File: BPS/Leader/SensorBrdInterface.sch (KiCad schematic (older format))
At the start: 15 parts, among them J7 MinionConn, J8 CurrentConn, U5 LTC6820, U6 LTC6820, U7 HX1188FNL

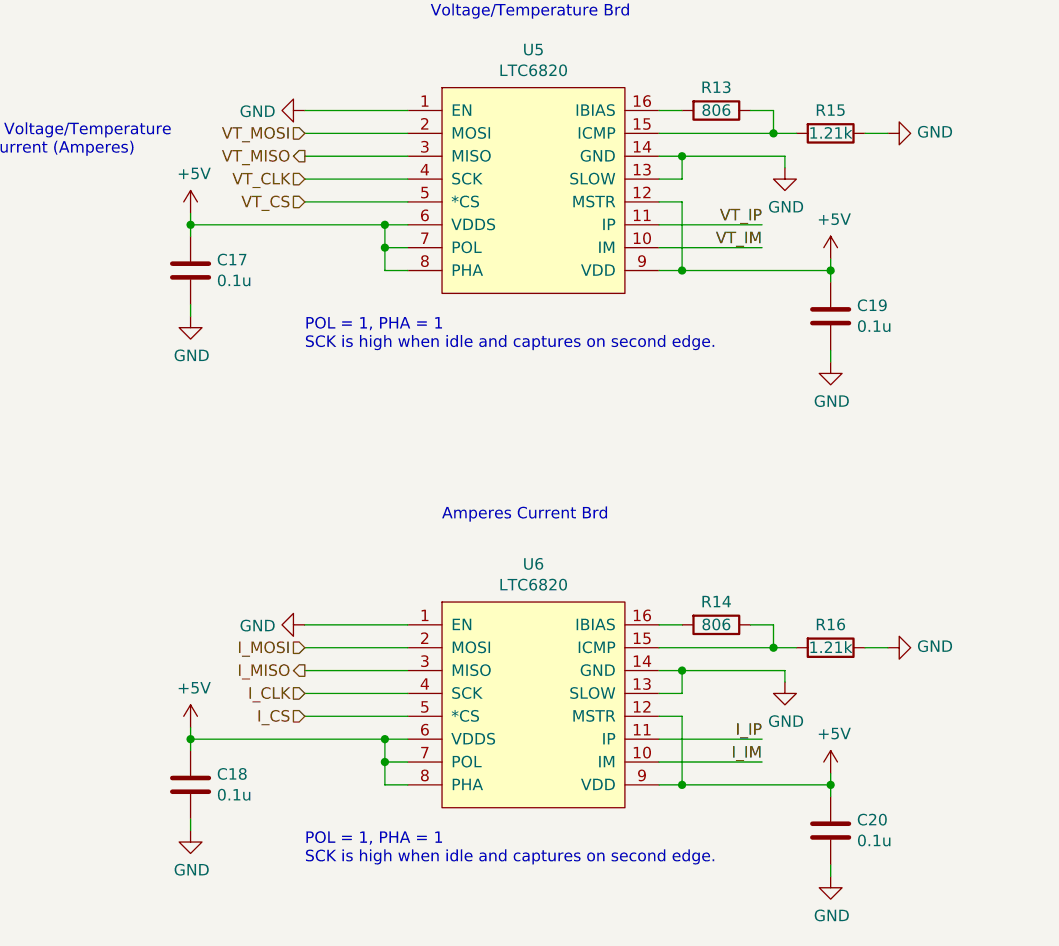
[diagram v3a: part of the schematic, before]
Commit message: Simplifies dc-dc converter schematics
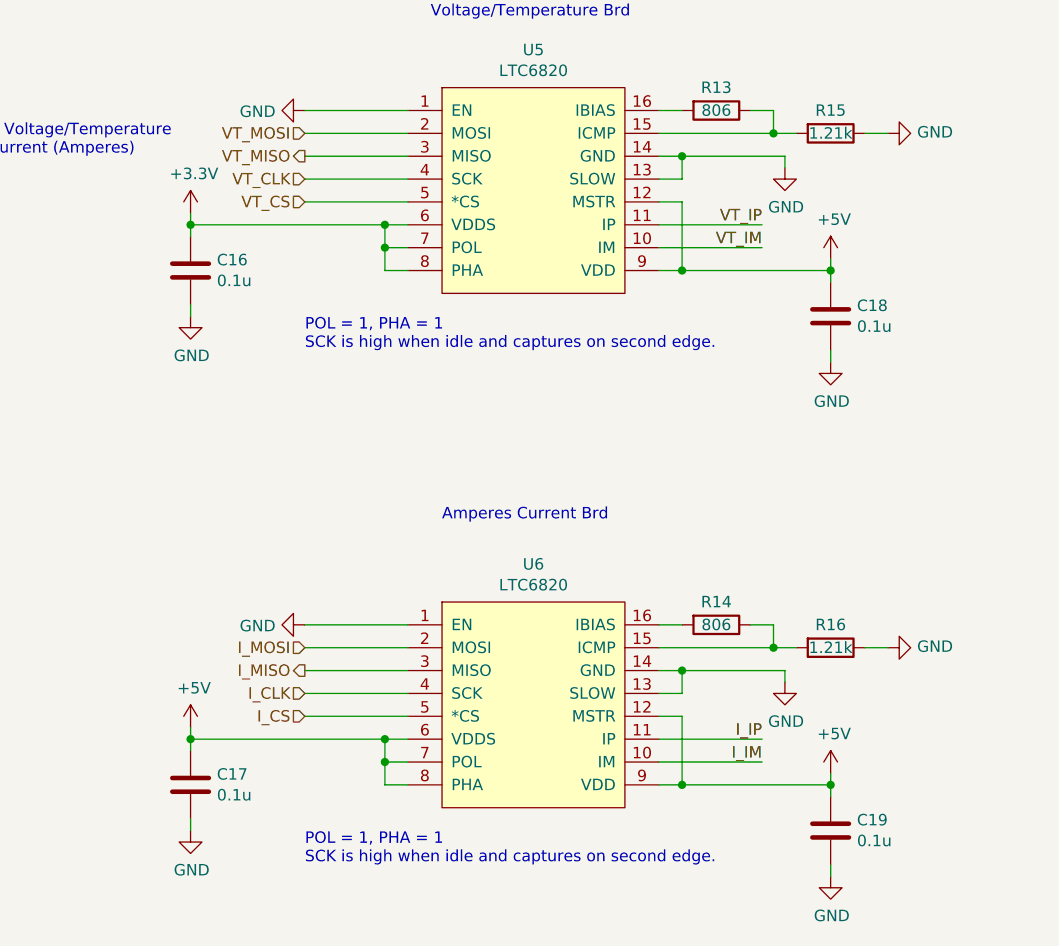
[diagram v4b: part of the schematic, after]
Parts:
- renumbered C17 to C16, C18 to C17, C19 to C18, C20 to C19
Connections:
- net +5V: no longer C16.1, U5.6 (VDDS), U5.7 (POL), U5.8 (PHA)
- new net +3V3: C16.1, U5.6 (VDDS), U5.7 (POL), U5.8 (PHA)
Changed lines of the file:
@@
 P 4650 2800
 AR Path="/5C4C7509/5D76E53B" Ref="#PWR?"  Part="1"
-AR Path="/5D766247/5D76E53B" Ref="#PWR041"  Part="1"
-F 0 "#PWR041" H 4650 2550 50  0001 C CNN
+AR Path="/5D766247/5D76E53B" Ref="#PWR040"  Part="1"
+F 0 "#PWR040" H 4650 2550 50  0001 C CNN
 F 1 "GND" H 4655 2627 50  0000 C CNN
 F 2 "" H 4650 2800 50  0001 C CNN
@@
 P 2550 2550
 AR Path="/5C4C7509/5D76E546" Ref="#PWR?"  Part="1"
-AR Path="/5D766247/5D76E546" Ref="#PWR039"  Part="1"
-F 0 "#PWR039" H 2550 2300 50  0001 C CNN
+AR Path="/5D766247/5D76E546" Ref="#PWR038"  Part="1"
+F 0 "#PWR038" H 2550 2300 50  0001 C CNN
 F 1 "GND" V 2555 2422 50  0000 R CNN
 F 2 "" H 2550 2550 50  0001 C CNN
@@
 P 2050 3250
 AR Path="/5C4C7509/5D76E54F" Ref="C?"  Part="1"
-AR Path="/5D766247/5D76E54F" Ref="C17"  Part="1"
-F 0 "C17" H 2165 3296 50  0000 L CNN
+AR Path="/5D766247/5D76E54F" Ref="C16"  Part="1"
+F 0 "C16" H 2165 3296 50  0000 L CNN
 F 1 "0.1u" H 2165 3205 50  0000 L CNN
 F 2 "Capacitor_SMD:C_0805_2012Metric" H 2088 3100 50  0001 C CNN
@@
 P 2050 3450
 AR Path="/5C4C7509/5D76E556" Ref="#PWR?"  Part="1"
-AR Path="/5D766247/5D76E556" Ref="#PWR036"  Part="1"
-F 0 "#PWR036" H 2050 3200 50  0001 C CNN
+AR Path="/5D766247/5D76E556" Ref="#PWR035"  Part="1"
+F 0 "#PWR035" H 2050 3200 50  0001 C CNN
 F 1 "GND" H 2055 3277 50  0000 C CNN
 F 2 "" H 2050 3450 50  0001 C CNN
@@
 P 4850 3450
 AR Path="/5C4C7509/5D76E56F" Ref="C?"  Part="1"
-AR Path="/5D766247/5D76E56F" Ref="C19"  Part="1"
-F 0 "C19" H 4965 3496 50  0000 L CNN
+AR Path="/5D766247/5D76E56F" Ref="C18"  Part="1"
+F 0 "C18" H 4965 3496 50  0000 L CNN
 F 1 "0.1u" H 4965 3405 50  0000 L CNN
 F 2 "Capacitor_SMD:C_0805_2012Metric" H 4888 3300 50  0001 C CNN
@@
 P 4850 3650
 AR Path="/5C4C7509/5D76E575" Ref="#PWR?"  Part="1"
-AR Path="/5D766247/5D76E575" Ref="#PWR044"  Part="1"
-F 0 "#PWR044" H 4850 3400 50  0001 C CNN
+AR Path="/5D766247/5D76E575" Ref="#PWR043"  Part="1"
+F 0 "#PWR043" H 4850 3400 50  0001 C CNN
 F 1 "GND" H 4855 3477 50  0000 C CNN
 F 2 "" H 4850 3650 50  0001 C CNN
@@
 P 5100 2650
 AR Path="/5C4C7509/5D76E58F" Ref="#PWR?"  Part="1"
-AR Path="/5D766247/5D76E58F" Ref="#PWR047"  Part="1"
-F 0 "#PWR047" H 5100 2400 50  0001 C CNN
+AR Path="/5D766247/5D76E58F" Ref="#PWR046"  Part="1"
+F 0 "#PWR046" H 5100 2400 50  0001 C CNN
 F 1 "GND" V 5105 2522 50  0000 R CNN
 F 2 "" H 5100 2650 50  0001 C CNN
@@
 P 4850 3200
 AR Path="/5C4C7509/5D76E5AC" Ref="#PWR?"  Part="1"
-AR Path="/5D766247/5D76E5AC" Ref="#PWR043"  Part="1"
-F 0 "#PWR043" H 4850 3050 50  0001 C CNN
+AR Path="/5D766247/5D76E5AC" Ref="#PWR042"  Part="1"
+F 0 "#PWR042" H 4850 3050 50  0001 C CNN
 F 1 "+5V" H 4865 3373 50  0000 C CNN
 F 2 "" H 4850 3200 50  0001 C CNN
@@
 Wire Wire Line
 	7100 3500 7500 3500
-$Comp
-L power:+5V #PWR?
-U 1 1 5D76E5D1
-P 2050 3000
-AR Path="/5C4C7509/5D76E5D1" Ref="#PWR?"  Part="1"
-AR Path="/5D766247/5D76E5D1" Ref="#PWR035"  Part="1"
-F 0 "#PWR035" H 2050 2850 50  0001 C CNN
-F 1 "+5V" H 2065 3173 50  0000 C CNN
-F 2 "" H 2050 3000 50  0001 C CNN
-F 3 "" H 2050 3000 50  0001 C CNN
-	1    2050 3000
-	1    0    0    -1
-$EndComp
 Wire Wire Line
 	2050 3000 2050 3050
@@
 P 4650 5050
 AR Path="/5C4C7509/5F151E6E" Ref="#PWR?"  Part="1"
-AR Path="/5D766247/5F151E6E" Ref="#PWR042"  Part="1"
-F 0 "#PWR042" H 4650 4800 50  0001 C CNN
+AR Path="/5D766247/5F151E6E" Ref="#PWR041"  Part="1"
+F 0 "#PWR041" H 4650 4800 50  0001 C CNN
 F 1 "GND" H 4655 4877 50  0000 C CNN
 F 2 "" H 4650 5050 50  0001 C CNN
@@
 P 2550 4800
 AR Path="/5C4C7509/5F151E76" Ref="#PWR?"  Part="1"
-AR Path="/5D766247/5F151E76" Ref="#PWR040"  Part="1"
-F 0 "#PWR040" H 2550 4550 50  0001 C CNN
+AR Path="/5D766247/5F151E76" Ref="#PWR039"  Part="1"
+F 0 "#PWR039" H 2550 4550 50  0001 C CNN
 F 1 "GND" V 2555 4672 50  0000 R CNN
 F 2 "" H 2550 4800 50  0001 C CNN
@@
 P 2050 5500
 AR Path="/5C4C7509/5F151E7F" Ref="C?"  Part="1"
-AR Path="/5D766247/5F151E7F" Ref="C18"  Part="1"
-F 0 "C18" H 2165 5546 50  0000 L CNN
+AR Path="/5D766247/5F151E7F" Ref="C17"  Part="1"
+F 0 "C17" H 2165 5546 50  0000 L CNN
 F 1 "0.1u" H 2165 5455 50  0000 L CNN
 F 2 "Capacitor_SMD:C_0805_2012Metric" H 2088 5350 50  0001 C CNN
@@
 P 2050 5700
 AR Path="/5C4C7509/5F151E86" Ref="#PWR?"  Part="1"
-AR Path="/5D766247/5F151E86" Ref="#PWR038"  Part="1"
-F 0 "#PWR038" H 2050 5450 50  0001 C CNN
+AR Path="/5D766247/5F151E86" Ref="#PWR037"  Part="1"
+F 0 "#PWR037" H 2050 5450 50  0001 C CNN
 F 1 "GND" H 2055 5527 50  0000 C CNN
 F 2 "" H 2050 5700 50  0001 C CNN
@@
 P 4850 5700
 AR Path="/5C4C7509/5F151E9F" Ref="C?"  Part="1"
-AR Path="/5D766247/5F151E9F" Ref="C20"  Part="1"
-F 0 "C20" H 4965 5746 50  0000 L CNN
+AR Path="/5D766247/5F151E9F" Ref="C19"  Part="1"
+F 0 "C19" H 4965 5746 50  0000 L CNN
 F 1 "0.1u" H 4965 5655 50  0000 L CNN
 F 2 "Capacitor_SMD:C_0805_2012Metric" H 4888 5550 50  0001 C CNN
@@
 P 4850 5900
 AR Path="/5C4C7509/5F151EA5" Ref="#PWR?"  Part="1"
-AR Path="/5D766247/5F151EA5" Ref="#PWR046"  Part="1"
-F 0 "#PWR046" H 4850 5650 50  0001 C CNN
+AR Path="/5D766247/5F151EA5" Ref="#PWR045"  Part="1"
+F 0 "#PWR045" H 4850 5650 50  0001 C CNN
 F 1 "GND" H 4855 5727 50  0000 C CNN
 F 2 "" H 4850 5900 50  0001 C CNN
@@
 P 5100 4900
 AR Path="/5C4C7509/5F151EBF" Ref="#PWR?"  Part="1"
-AR Path="/5D766247/5F151EBF" Ref="#PWR048"  Part="1"
-F 0 "#PWR048" H 5100 4650 50  0001 C CNN
+AR Path="/5D766247/5F151EBF" Ref="#PWR047"  Part="1"
+F 0 "#PWR047" H 5100 4650 50  0001 C CNN
 F 1 "GND" V 5105 4772 50  0000 R CNN
 F 2 "" H 5100 4900 50  0001 C CNN
@@
 P 4850 5450
 AR Path="/5C4C7509/5F151EC9" Ref="#PWR?"  Part="1"
-AR Path="/5D766247/5F151EC9" Ref="#PWR045"  Part="1"
-F 0 "#PWR045" H 4850 5300 50  0001 C CNN
+AR Path="/5D766247/5F151EC9" Ref="#PWR044"  Part="1"
+F 0 "#PWR044" H 4850 5300 50  0001 C CNN
 F 1 "+5V" H 4865 5623 50  0000 C CNN
 F 2 "" H 4850 5450 50  0001 C CNN
@@
 P 2050 5250
 AR Path="/5C4C7509/5F151ED3" Ref="#PWR?"  Part="1"
-AR Path="/5D766247/5F151ED3" Ref="#PWR037"  Part="1"
-F 0 "#PWR037" H 2050 5100 50  0001 C CNN
+AR Path="/5D766247/5F151ED3" Ref="#PWR036"  Part="1"
+F 0 "#PWR036" H 2050 5100 50  0001 C CNN
 F 1 "+5V" H 2065 5423 50  0000 C CNN
 F 2 "" H 2050 5250 50  0001 C CNN
@@
 $EndComp
 $Comp
-L power:+12V #PWR049
+L power:+12V #PWR048
 U 1 1 5F1F84DF
 P 9100 4000
-F 0 "#PWR049" H 9100 3850 50  0001 C CNN
+F 0 "#PWR048" H 9100 3850 50  0001 C CNN
 F 1 "+12V" H 9115 4173 50  0000 C CNN
 F 2 "" H 9100 4000 50  0001 C CNN
@@
 $EndComp
 $Comp
-L power:GNDPWR #PWR050
+L power:GNDPWR #PWR049
 U 1 1 5F1F8DBA
 P 9100 4500
-F 0 "#PWR050" H 9100 4300 50  0001 C CNN
+F 0 "#PWR049" H 9100 4300 50  0001 C CNN
 F 1 "GNDPWR" H 9104 4346 50  0000 C CNN
 F 2 "" H 9100 4450 50  0001 C CNN
@@
 Text Notes 2650 1900 0    50   ~ 10
 4-wire SPI to 2-wire Isolated SPI Converter ICs
+$Comp
+L power:+3.3V #PWR034
+U 1 1 5F1D7210
+P 2050 3000
+F 0 "#PWR034" H 2050 2850 50  0001 C CNN
+F 1 "+3.3V" H 2065 3173 50  0000 C CNN
+F 2 "" H 2050 3000 50  0001 C CNN
+F 3 "" H 2050 3000 50  0001 C CNN
+	1    2050 3000
+	1    0    0    -1
+$EndComp
 $EndSCHEMATC

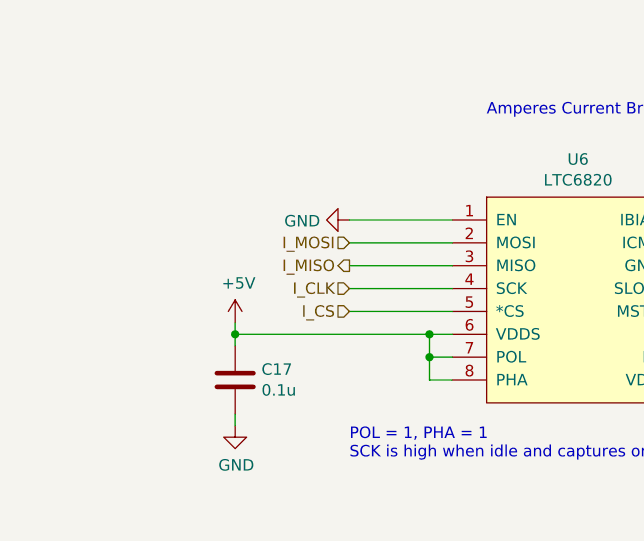
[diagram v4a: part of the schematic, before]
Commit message: Finishes new power circuitry tracing
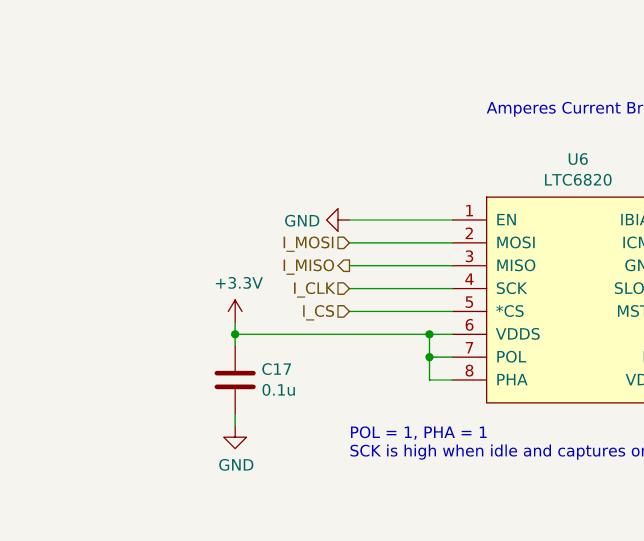
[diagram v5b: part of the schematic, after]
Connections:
- net +3V3: now also C17.1, U6.6 (VDDS), U6.7 (POL), U6.8 (PHA)
- net +5V: no longer C17.1, U6.6 (VDDS), U6.7 (POL), U6.8 (PHA)
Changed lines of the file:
@@
 Wire Wire Line
 	2900 5500 3000 5500
-$Comp
-L power:+5V #PWR?
-U 1 1 5F151ED3
-P 2050 5250
-AR Path="/5C4C7509/5F151ED3" Ref="#PWR?"  Part="1"
-AR Path="/5D766247/5F151ED3" Ref="#PWR036"  Part="1"
-F 0 "#PWR036" H 2050 5100 50  0001 C CNN
-F 1 "+5V" H 2065 5423 50  0000 C CNN
-F 2 "" H 2050 5250 50  0001 C CNN
-F 3 "" H 2050 5250 50  0001 C CNN
-	1    2050 5250
-	1    0    0    -1
-$EndComp
 Wire Wire Line
 	2050 5250 2050 5300
@@
 	1    0    0    -1
 $EndComp
+$Comp
+L power:+3.3V #PWR0104
+U 1 1 5F1DCEE5
+P 2050 5250
+F 0 "#PWR0104" H 2050 5100 50  0001 C CNN
+F 1 "+3.3V" H 2065 5423 50  0000 C CNN
+F 2 "" H 2050 5250 50  0001 C CNN
+F 3 "" H 2050 5250 50  0001 C CNN
+	1    2050 5250
+	1    0    0    -1
+$EndComp

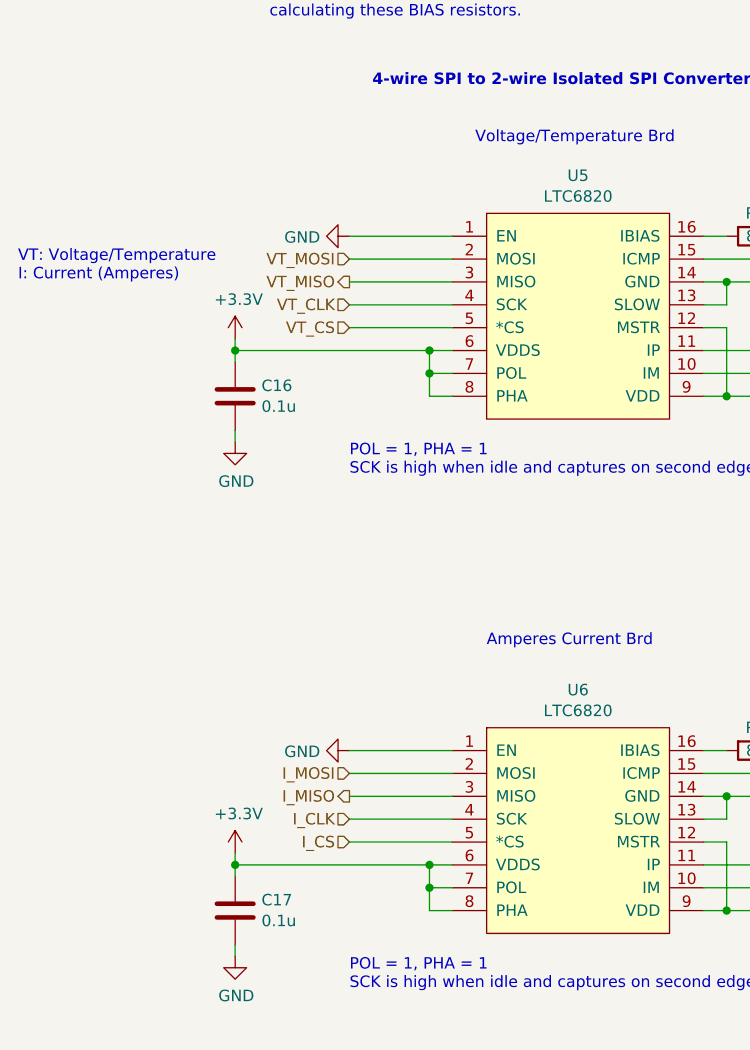
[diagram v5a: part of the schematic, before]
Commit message: Changes LTC6820 POL and PHA pins to +5V due to VIH and VIL parameters in datasheet
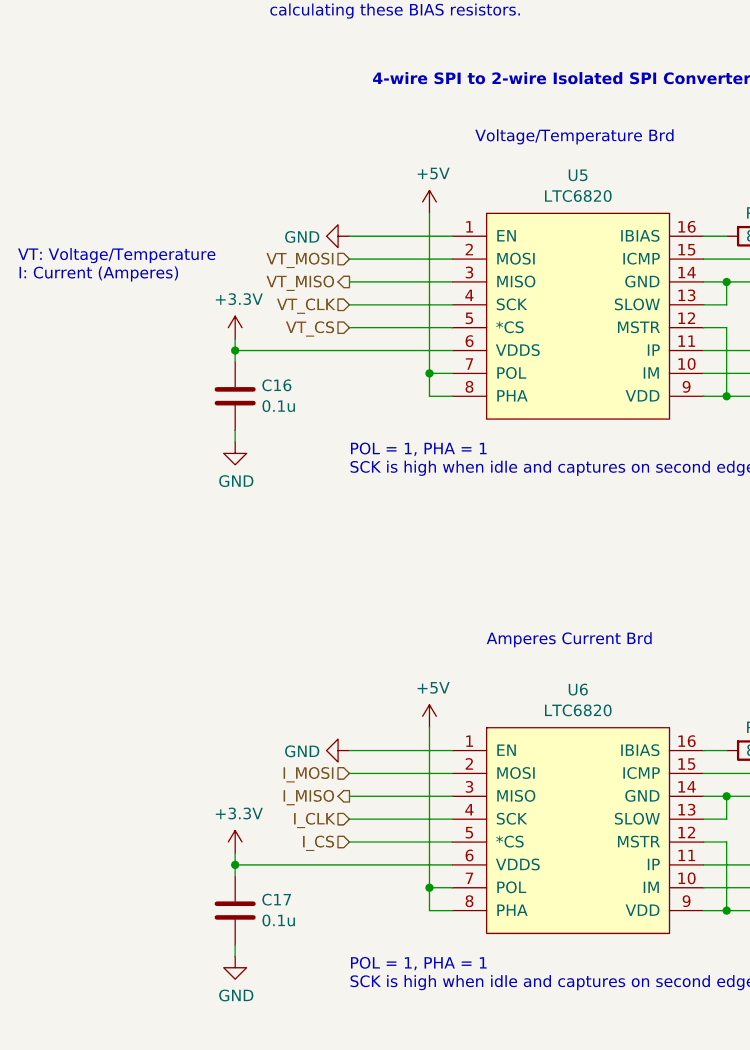
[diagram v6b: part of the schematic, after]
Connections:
- net +3V3: no longer U5.7 (POL), U5.8 (PHA), U6.7 (POL), U6.8 (PHA)
- net +5V: now also U5.7 (POL), U5.8 (PHA), U6.7 (POL), U6.8 (PHA)
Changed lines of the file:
@@
 NoConn ~ 7500 3600
-Wire Wire Line
-	2050 3050 2900 3050
 Wire Wire Line
 	3000 3150 2900 3150
@@
 	2050 3000 2050 3050
 Connection ~ 2050 3050
-Wire Wire Line
-	2900 3150 2900 3050
-Connection ~ 2900 3150
-Connection ~ 2900 3050
-Wire Wire Line
-	2900 3050 3000 3050
 $Comp
 L Device:R_Small R?
@@
 $EndComp
 Wire Wire Line
-	2050 5300 2900 5300
-Wire Wire Line
 	3000 5400 2900 5400
 Wire Wire Line
@@
 	2050 5250 2050 5300
 Connection ~ 2050 5300
-Wire Wire Line
-	2900 5400 2900 5300
-Connection ~ 2900 5400
-Connection ~ 2900 5300
-Wire Wire Line
-	2900 5300 3000 5300
 Wire Wire Line
 	2550 2750 3000 2750
@@
 	1    0    0    -1
 $EndComp
+Wire Wire Line
+	2050 3050 3000 3050
+$Comp
+L power:+5V #PWR?
+U 1 1 5F27160B
+P 2900 2450
+AR Path="/5C4C7509/5F27160B" Ref="#PWR?"  Part="1"
+AR Path="/5D766247/5F27160B" Ref="#PWR?"  Part="1"
+F 0 "#PWR?" H 2900 2300 50  0001 C CNN
+F 1 "+5V" H 2915 2623 50  0000 C CNN
+F 2 "" H 2900 2450 50  0001 C CNN
+F 3 "" H 2900 2450 50  0001 C CNN
+	1    2900 2450
+	1    0    0    -1
+$EndComp
+Wire Wire Line
+	2900 2450 2900 3150
+Connection ~ 2900 3150
+Wire Wire Line
+	2050 5300 3000 5300
+$Comp
+L power:+5V #PWR?
+U 1 1 5F27542F
+P 2900 4700
+AR Path="/5C4C7509/5F27542F" Ref="#PWR?"  Part="1"
+AR Path="/5D766247/5F27542F" Ref="#PWR?"  Part="1"
+F 0 "#PWR?" H 2900 4550 50  0001 C CNN
+F 1 "+5V" H 2915 4873 50  0000 C CNN
+F 2 "" H 2900 4700 50  0001 C CNN
+F 3 "" H 2900 4700 50  0001 C CNN
+	1    2900 4700
+	1    0    0    -1
+$EndComp
+Wire Wire Line
+	2900 4700 2900 5400
+Connection ~ 2900 5400
 $EndSCHEMATC
